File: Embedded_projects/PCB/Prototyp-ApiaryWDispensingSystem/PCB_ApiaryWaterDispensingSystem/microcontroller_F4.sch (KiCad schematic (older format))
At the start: 39 parts

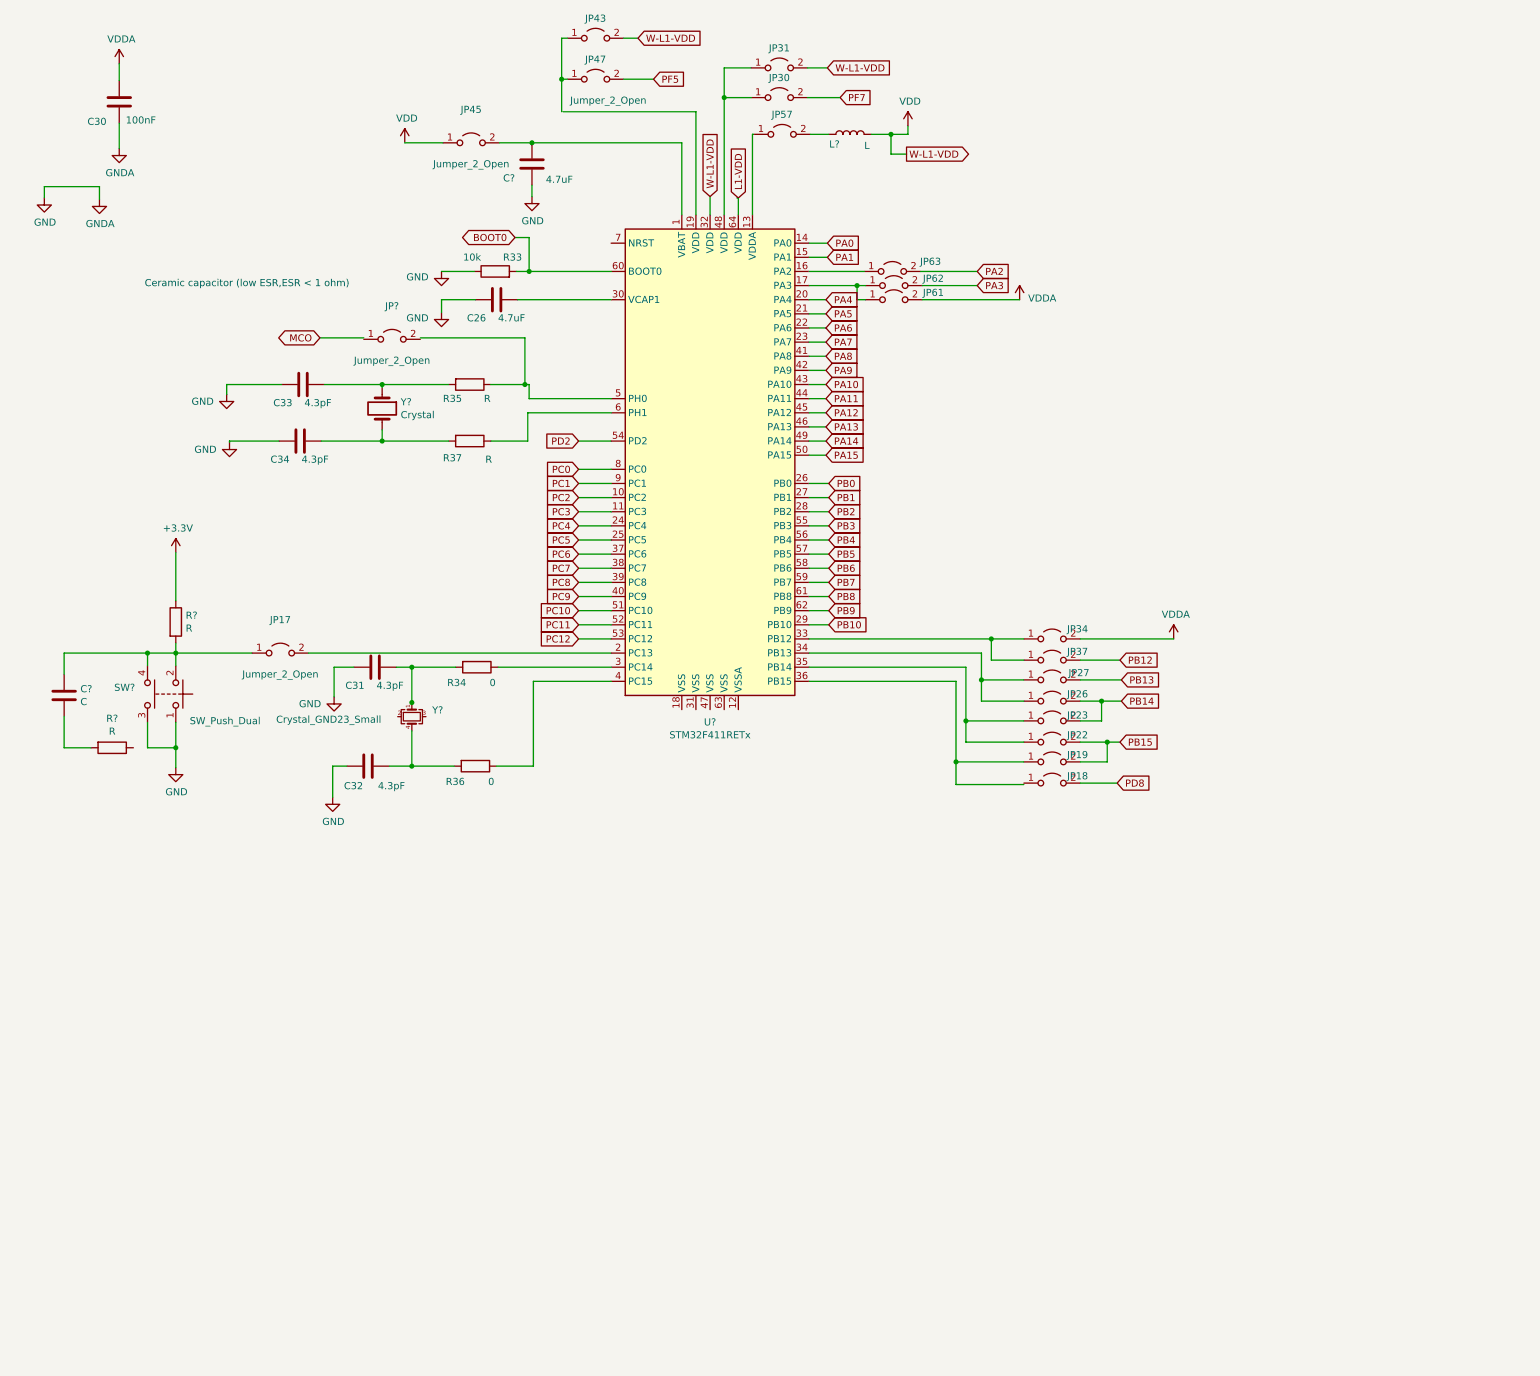
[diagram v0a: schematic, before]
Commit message: stm32f411re completed schematic
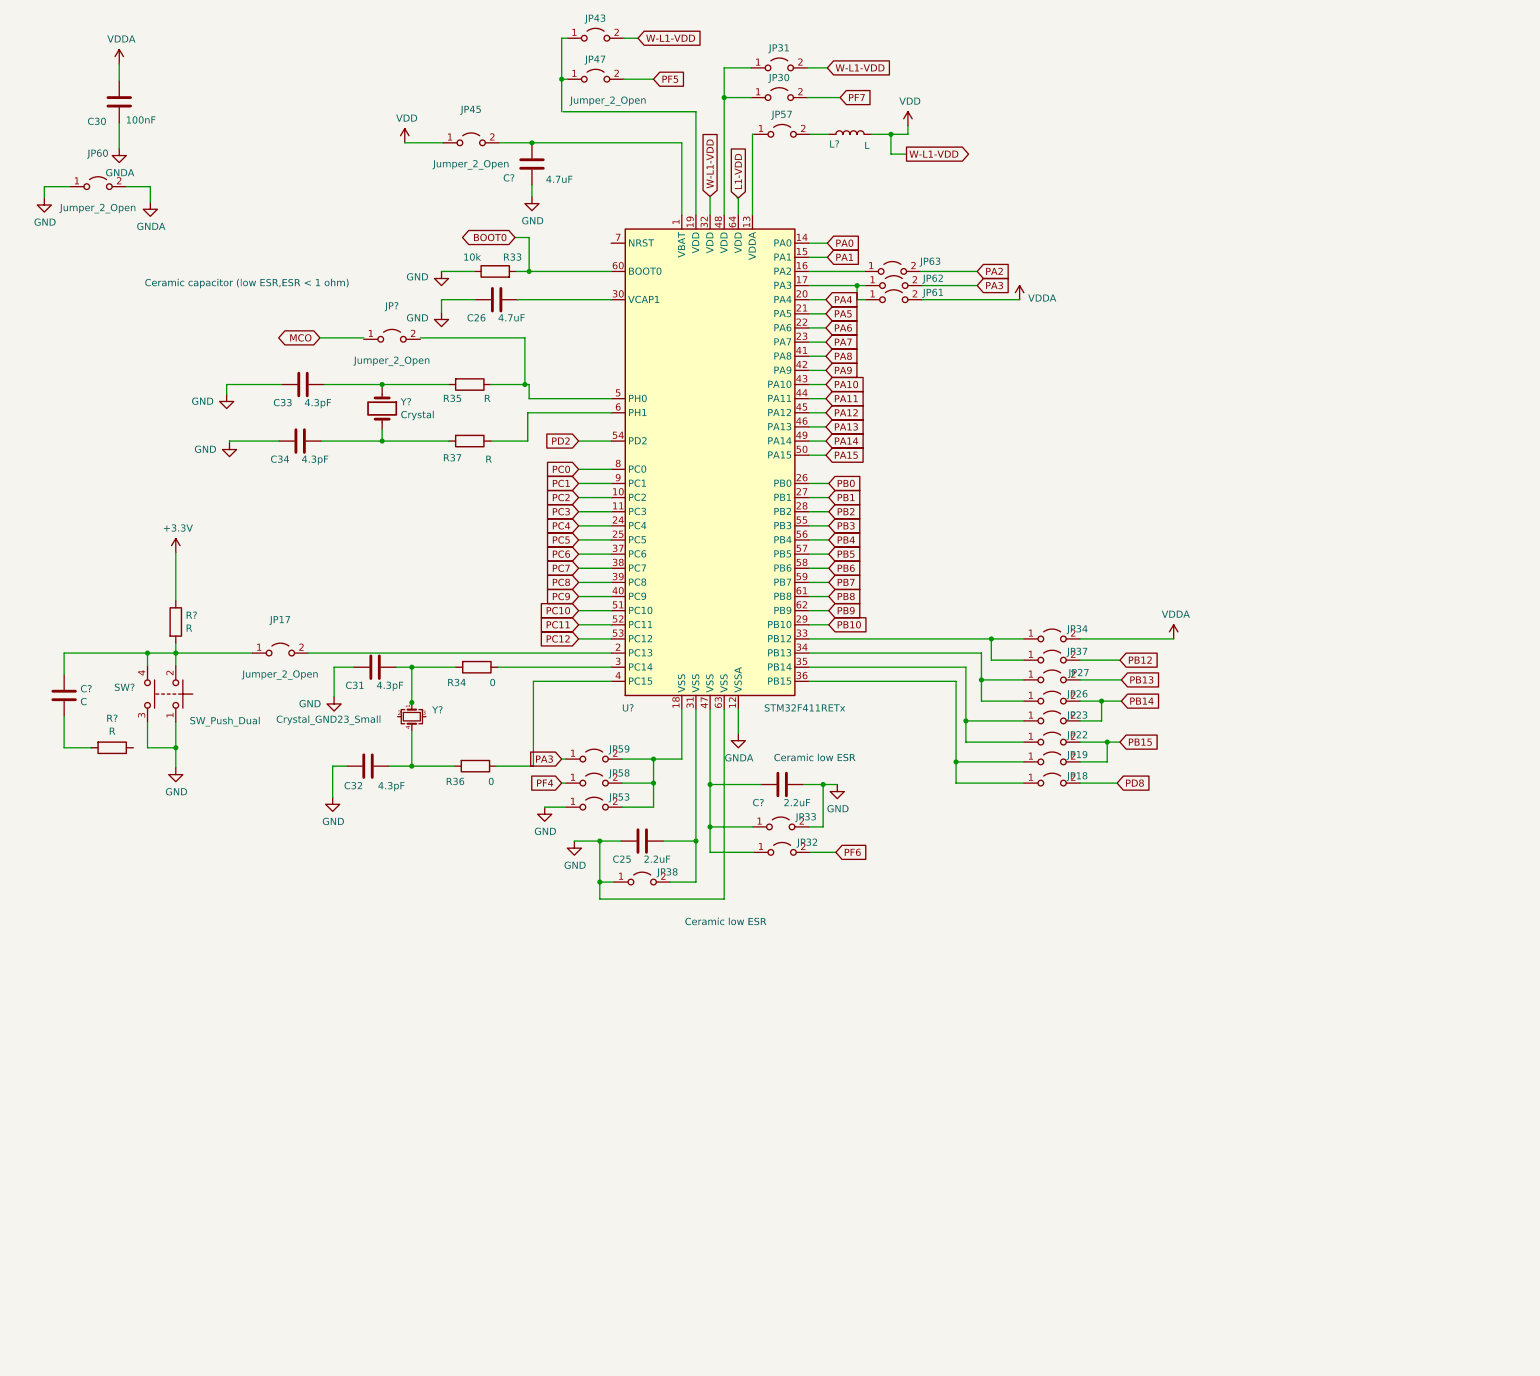
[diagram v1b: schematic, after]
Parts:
- added C25, C?: 2.2uF, symbol Device:C
- added JP32, JP33, JP38, JP53, JP58, JP59, JP60: Jumper_2_Open, Jumper:SolderJumper-2_P1.3mm_Open_TrianglePad1.0x1.5mm, symbol Jumper:Jumper_2_Open
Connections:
- net labels added: PF4, PF6
- wire segments 171 -> 205
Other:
- note added: "Ceramic low ESR"

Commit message: added changes of Microntroller_F4 ->global variables #3
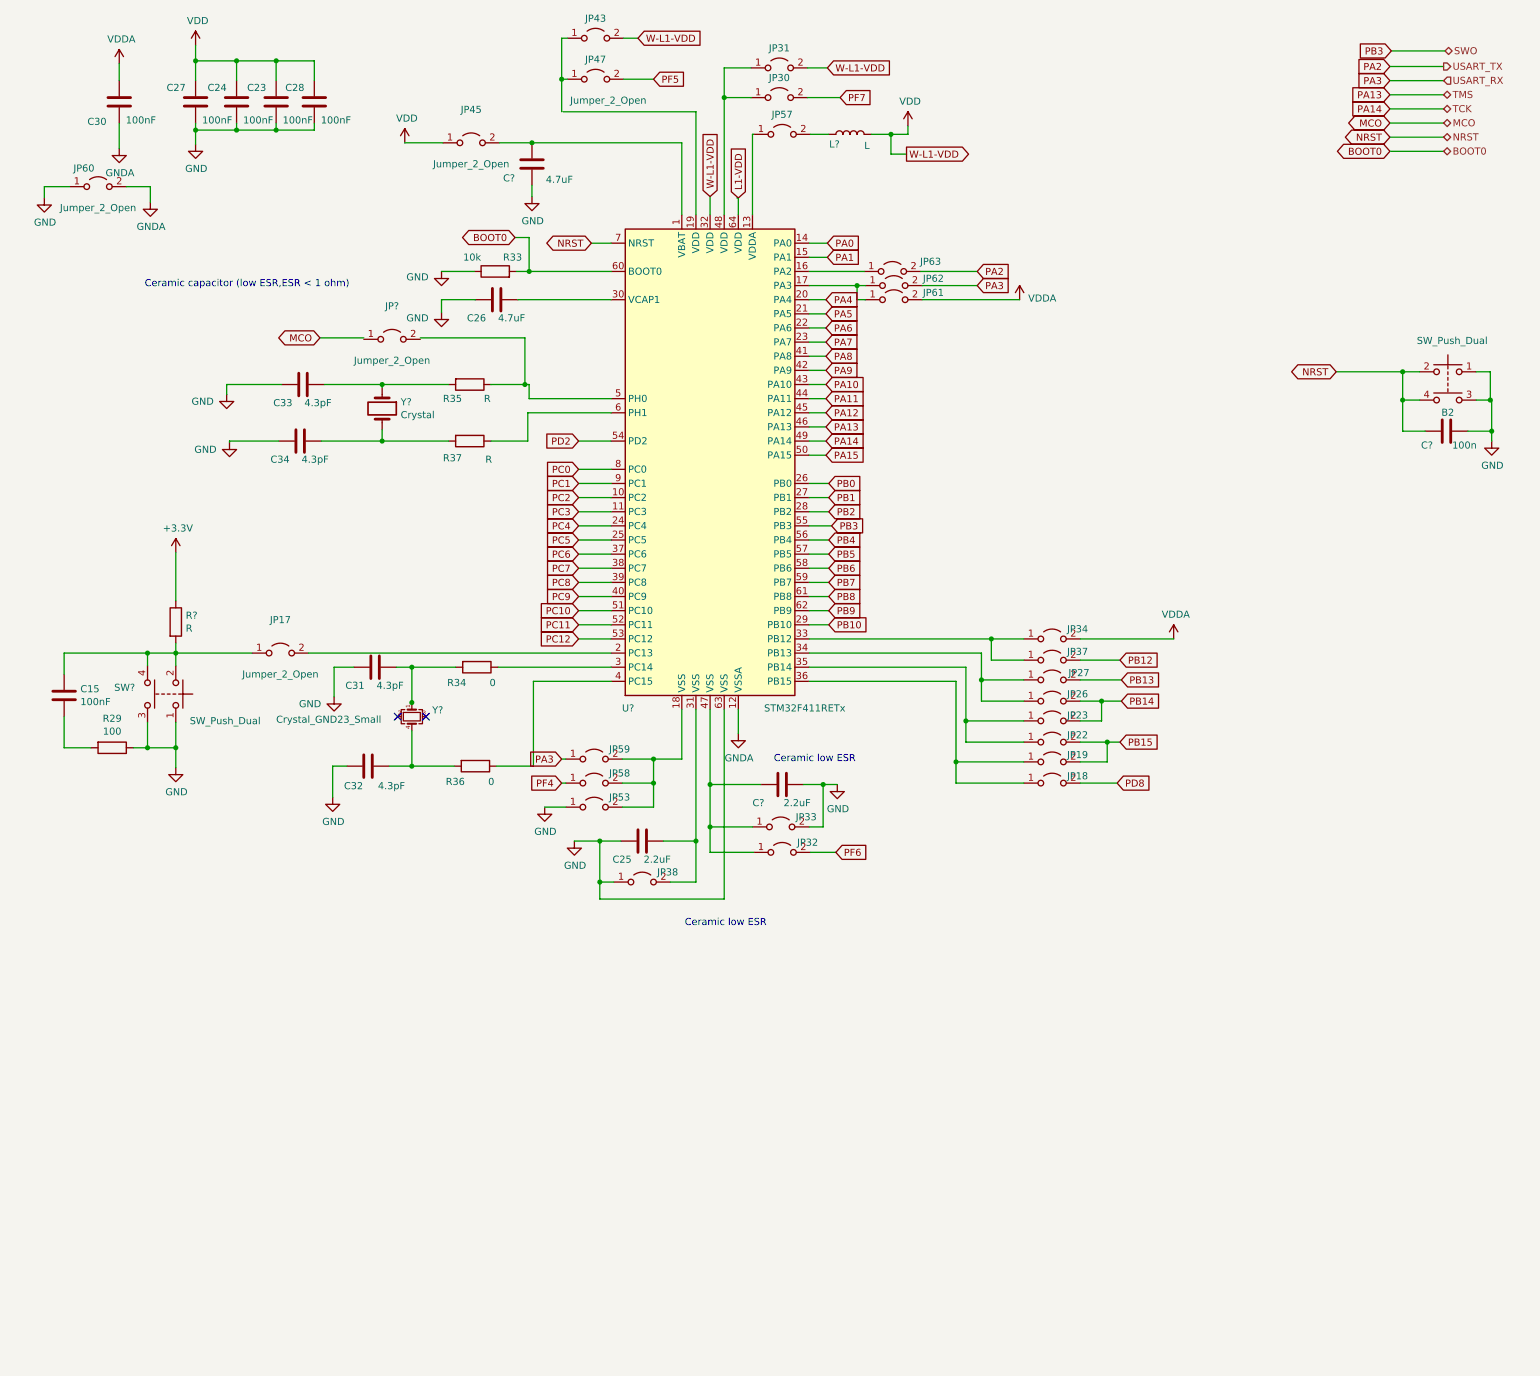
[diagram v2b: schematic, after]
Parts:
- added B2: SW_Push_Dual, symbol Switch:SW_Push_Dual
- added C23, C24, C27, C28: 100nF, symbol Device:C
- added C?: 100n, symbol Device:C
- C15: renamed from C?; value C -> 100nF
- R29: renamed from R?; value R -> 100
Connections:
- net GND: now also R29.1, B2.1, B2.3, C23.1, C24.1, C27.1, C28.1, C?.1
- net VDD: now also C23.2, C24.2, C27.2, C28.2
- net NRST: now reaches U?.7 (NRST)
- net NRST: now also B2.2, B2.4, C?.2
- no-connect marks 0 -> 2

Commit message: added lot of changes to project #3
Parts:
- added J10, J7: Conn_02x19_Odd_Even, symbol Connector_Generic:Conn_02x19_Odd_Even
- added JP20, JP24, JP25, JP28, JP29, JP35, JP36, JP39, JP40, JP41, JP42, JP44, JP48, JP49, JP51, JP54, JP55, JP56, JP64, JP65: Jumper_2_Open, Jumper:SolderJumper-2_P1.3mm_Open_TrianglePad1.0x1.5mm, symbol Jumper:Jumper_2_Open
- B2: footprint (none) -> Button_Switch_SMD:SW_Push_1P1T_NO_6x6mm_H9.5mm
- C14: renamed from C?; footprint (none) -> Capacitor_SMD:C_0805_2012Metric
- C15, C23, C24, C27, C28, C30, C31, C32, C33, C34, R35, R37: footprint (none) -> Capacitor_SMD:C_0805_2012Metric
- C22: renamed from C?; footprint (none) -> Capacitor_SMD:C_1206_3216Metric
- C25: footprint (none) -> Capacitor_SMD:C_1206_3216Metric
- C26: footprint (none) -> Capacitor_SMD:C_0603_1608Metric
- C29: renamed from C?; value 4.7uF -> 1 uF_X5R_0603; footprint (none) -> Capacitor_SMD:C_0603_1608Metric
- L?: footprint (none) -> Inductor_SMD:L_0805_2012Metric
- R29, R33, R34, R36: footprint (none) -> Resistor_SMD:R_0805_2012Metric
- R30: renamed from R?; value R -> 4k7
- SW1: renamed from SW?; footprint (none) -> Button_Switch_SMD:SW_Push_1P1T_NO_6x6mm_H9.5mm
- Y3: renamed from Y?; footprint (none) -> Crystal:Resonator-2Pin_W8.0mm_H3.5mm
- gave numbers to parts that had none: 2
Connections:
- net +3V3 is gone; now on net VDD: R30.1
- net BOOT0: now also J7.7 (Pin_7)
- net GND: now also J10.20 (Pin_20), J10.9 (Pin_9), J7.19 (Pin_19), J7.20 (Pin_20), J7.22 (Pin_22), J7.8 (Pin_8)
- net GNDA: now also J10.32 (Pin_32)
- net MCO: now also JP50.1 (A)
- net NRST: now also J7.14 (Pin_14)
- net PA0: now also J7.28 (Pin_28)
- net PA1: now also J7.30 (Pin_30)
- net PA10: now also J10.33 (Pin_33)
- net PA11: now also J10.14 (Pin_14)
- net PA12: now also J10.12 (Pin_12)
- net PA13: now also J7.13 (Pin_13)
- net PA14: now also J7.15 (Pin_15)
- net PA15: now also J7.17 (Pin_17)
- net PA2: now also J10.35 (Pin_35)
- net PA3: now also J10.37 (Pin_37)
- net PA4: now also J7.32 (Pin_32)
- net PA5: now also JP42.1 (A), JP44.1 (A)
- net PA6: now also JP39.1 (A), JP41.1 (A)
- net PA7: now also JP36.1 (A), JP40.1 (A)
- net PA8: now also J10.23 (Pin_23)
- net PA9: now also J10.21 (Pin_21)
- net PB0: now also J7.34 (Pin_34)
- net PB1: now also J10.24 (Pin_24), JP64.2 (B); no longer U?.27 (PB1)
- net PB10: now also J10.25 (Pin_25)
- net PB12: now also J10.16 (Pin_16)
- net PB13: now also JP29.2 (B), JP35.2 (B)
- net PB14: now also JP24.2 (B), JP28.2 (B)
- net PB15: now also JP20.2 (B), JP25.2 (B)
- net PB2: now also J10.22 (Pin_22)
- net PB3: now also J10.31 (Pin_31)
- net PB4: now also J10.27 (Pin_27)
- net PB5: now also J10.29 (Pin_29)
- net PB6: now also J10.17 (Pin_17)
- net PB7: now also J7.21 (Pin_21)
- net PB8: now also J10.3 (Pin_3)
- net PB9: now also J10.5 (Pin_5)
- net PC0: now also JP51.1 (A)
- net PC1: now also JP56.1 (A)
- net PC10: now also J7.1 (Pin_1)
- net PC11: now also J7.2 (Pin_2)
- net PC12: now also J7.3 (Pin_3)
- net PC2: now also J7.35 (Pin_35)
- net PC3: now also J7.37 (Pin_37)
- net PC4: now also J10.34 (Pin_34)
- net PC5: now also J10.6 (Pin_6)
- net PC6: now also J10.4 (Pin_4)
- net PC7: now also J10.19 (Pin_19)
- net PC8: now also J10.2 (Pin_2)
- net PC9: now also J10.1 (Pin_1)
- net PD2: now also J7.4 (Pin_4)
- net PD8: now also J10.10 (Pin_10)
- net PF4: now also J10.38 (Pin_38)
- net PF5: now also J10.36 (Pin_36)
- net PF6: now also J7.9 (Pin_9)
- net PF7: now also J7.11 (Pin_11)
- net VDD: now also J7.12 (Pin_12), J7.16 (Pin_16), J7.5 (Pin_5)
- net VDDA: now also JP57.1 (A), U?.13 (VDDA), J10.7 (Pin_7), JP65.2 (B)
- net at U?.19 (VDD): now also JP43.1 (A), JP47.1 (A)
- net at R35.1, U?.5 (PH0): now also JP50.2 (B)
- new net: JP64.1 (A), JP65.1 (A), U?.27 (PB1)
- new net: J7.25 (Pin_25), JP49.1 (A)
- new net: J7.27 (Pin_27), JP48.1 (A)
- new net: J7.29 (Pin_29), JP55.1 (A)
- new net: J7.31 (Pin_31), JP54.1 (A)
- new net: J7.36 (Pin_36), JP56.2 (B)
- new net: J7.38 (Pin_38), JP51.2 (B)
- new net +5V: J7.18 (Pin_18)
- new net +5VA: J7.6 (Pin_6)
- new net +5VP: J10.8 (Pin_8)
- new net +BATT: J7.33 (Pin_33)
- new net +VDC: J7.24 (Pin_24)
- new net D11: J10.15 (Pin_15), JP20.1 (A), JP40.2 (B)
- new net D12: J10.13 (Pin_13), JP24.1 (A), JP41.2 (B)
- new net D13: J10.11 (Pin_11), JP29.1 (A), JP42.2 (B)
- new net J10_CN26: J10.26 (Pin_26), JP25.1 (A), JP36.2 (B)
- new net J10_CN28: J10.28 (Pin_28), JP28.1 (A), JP39.2 (B)
- new net J10_CN30: J10.30 (Pin_30), JP35.1 (A), JP44.2 (B)
- new net PB11: J10.18 (Pin_18)
- new net PC13: J7.23 (Pin_23)
- new net PC14: JP49.2 (B)
- new net PC15: JP48.2 (B)
- new net PF0: JP55.2 (B)
- new net PF1: JP54.2 (B)
- no-connect marks 2 -> 4
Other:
- note added: "Buttons connections"
- note added: "Digital connections UART"
- note added: "I2C Connection"
- note added: "JP20, JP24, JP29, \nOpen only for F302"
- note added: "JP25, JP28, JP35, \nOpen only for F302"
- note added: "Motor Control"
- note added: "RESET BUTTON"
- note added: "SPI Connections"
- note added: "USER BUTTON"
- moved on the sheet: B2, C14, C15, C22, C23, C24, C25, C26, C27, C28, C29, C30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

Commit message: Many design changes have been added over the past few months #3
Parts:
- added JP?: Jumper_2_Open, Jumper:SolderJumper-2_P1.3mm_Open_TrianglePad1.0x1.5mm, symbol Jumper:Jumper_2_Open
- C14, C15, C23, C24, C27, C28, C30, C31, C32, C33, C34: footprint Capacitor_SMD:C_0805_2012Metric -> Capacitor_SMD:C_0603_1608Metric
- C26: footprint Capacitor_SMD:C_0603_1608Metric -> Capacitor_SMD:C_0805_2012Metric
- L?: footprint Inductor_SMD:L_0805_2012Metric -> Inductor_SMD:L_0603_1608Metric
- R29, R33, R34, R36: footprint Resistor_SMD:R_0805_2012Metric -> Resistor_SMD:R_0603_1608Metric
- R30: footprint (none) -> Resistor_SMD:R_0603_1608Metric
- R35, R37: footprint Capacitor_SMD:C_0805_2012Metric -> Resistor_SMD:R_0603_1608Metric
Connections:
- net L1-VDD is gone; now on net VDD: U?.64 (VDD)
- net at C29.2, JP45.2 (B), U?.1 (VBAT): now also JP?.2 (B)
- net +BATT renamed BAT
- net BAT: now also JP?.1 (A)
- net +VDC renamed VM
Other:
- note added: "ADC Connections"
- note added: "POWER SUPPLY"
- moved on the sheet: C23, C24, C27, C28, C30, JP60
